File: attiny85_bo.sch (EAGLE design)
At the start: 11 parts, among them IC1 ATTiny85, J1 AVR_SPI_PRG_6NS, Y1 16MHz

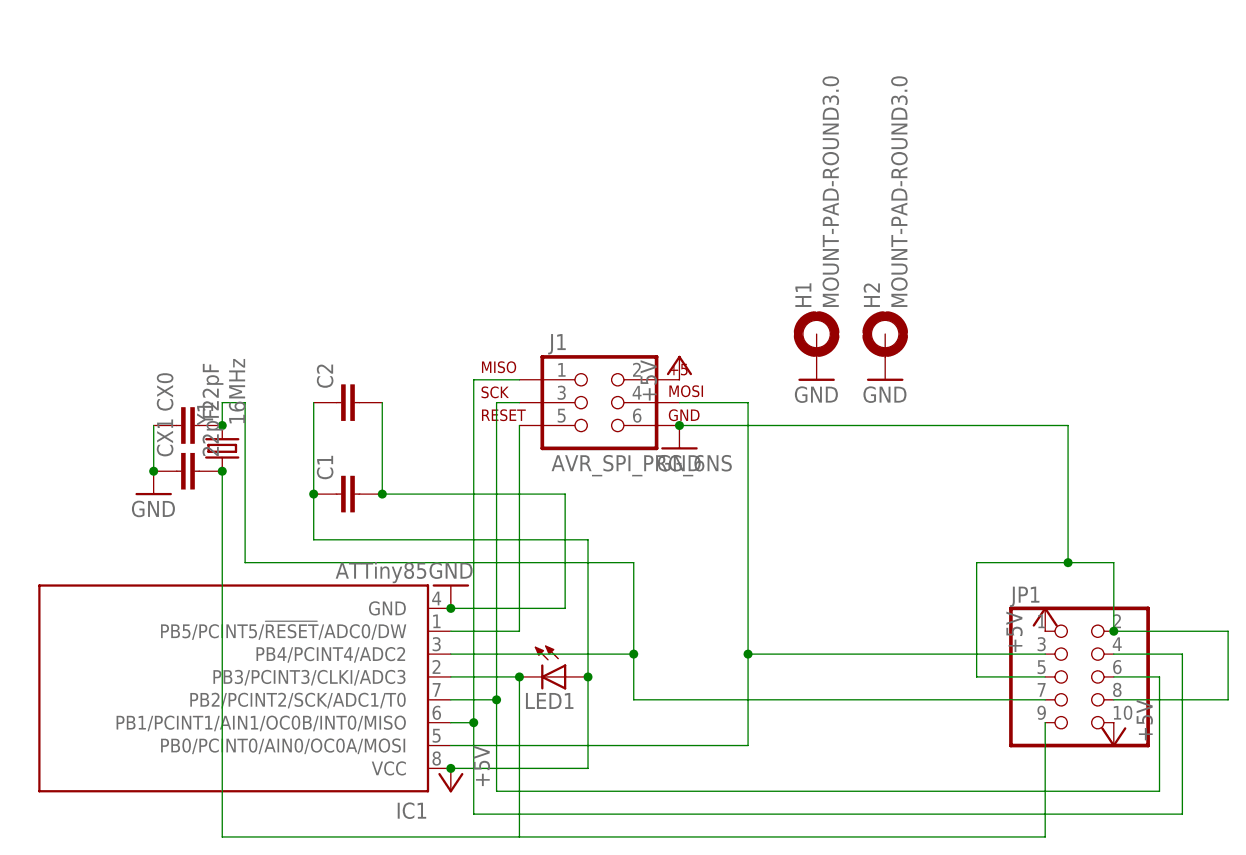
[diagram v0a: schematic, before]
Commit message: remaking the attiny85 baord so it is more easily connected to stripboard via 90deg pin header
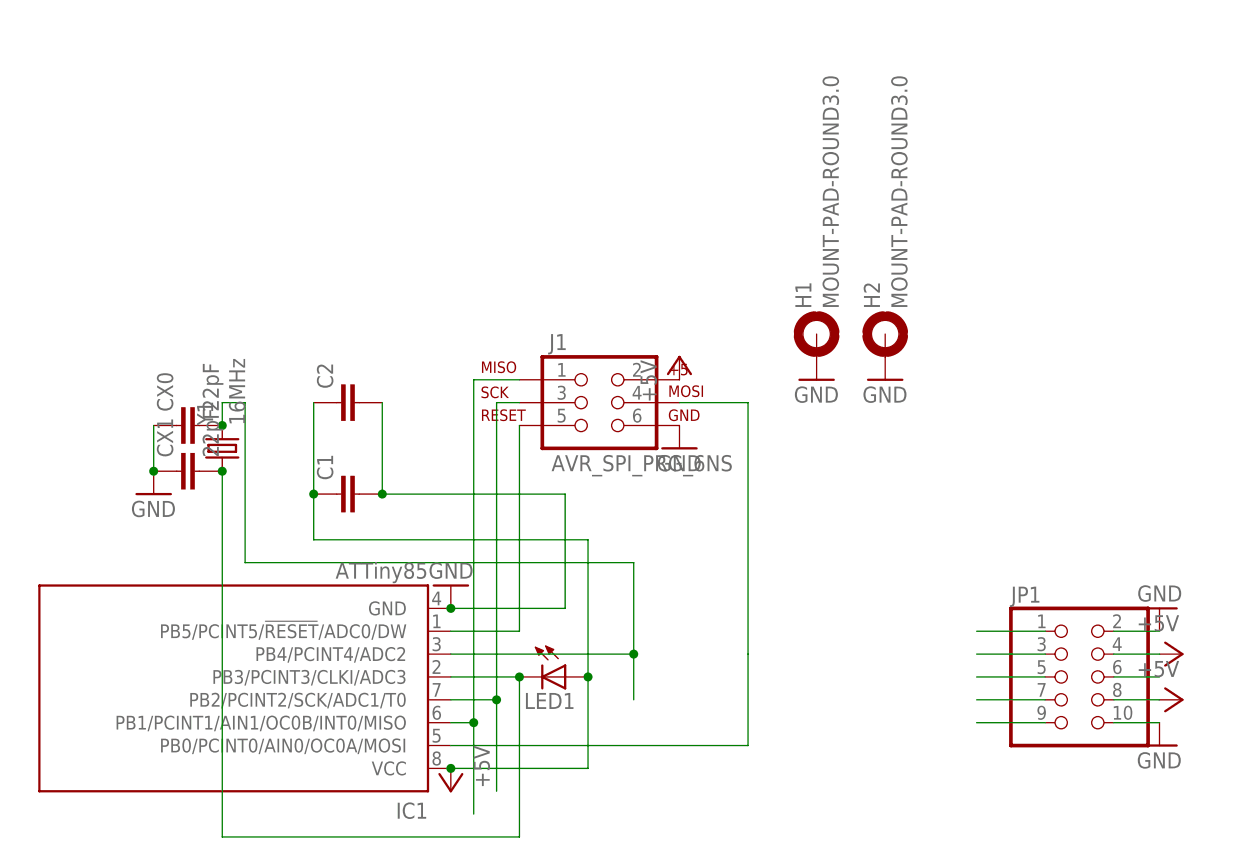
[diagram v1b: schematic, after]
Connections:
- net +5V: now also JP1.4, JP1.8; no longer JP1.1, JP1.10
- net GND: now also JP1.10; no longer JP1.5, JP1.8
- net PB0: now also JP1.1; no longer JP1.3
- net PB1: now also JP1.3; no longer JP1.4
- net PB2: now also JP1.5; no longer JP1.6
- net PB3: now also JP1.7; no longer JP1.9
- net PB4: now also JP1.9; no longer JP1.7
- net PB5: now also JP1.6
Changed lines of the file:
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@@
 <?xml version="1.0" encoding="utf-8"?>
 <!DOCTYPE eagle SYSTEM "eagle.dtd">
-<eagle version="6.2">
+<eagle version="6.4">
 <drawing>
 <settings>
@@
 <part name="GND1" library="supply1" deviceset="GND" device=""/>
 <part name="GND2" library="supply1" deviceset="GND" device=""/>
-<part name="P+1" library="supply1" deviceset="+5V" device=""/>
-<part name="P+2" library="supply1" deviceset="+5V" device=""/>
 <part name="CX0" library="rcl" deviceset="C-EU" device="C0603" value="22pF"/>
 <part name="CX1" library="rcl" deviceset="C-EU" device="C0603" value="22pF"/>
 <part name="GND4" library="supply1" deviceset="GND" device=""/>
 <part name="Y1" library="SparkFun-FreqCtrl" deviceset="CRYSTAL" device="5X3" value="16MHz"/>
+<part name="GND6" library="supply1" deviceset="GND" device=""/>
+<part name="GND7" library="supply1" deviceset="GND" device=""/>
+<part name="P+1" library="supply1" deviceset="+5V" device=""/>
+<part name="P+2" library="supply1" deviceset="+5V" device=""/>
 </parts>
 <sheets>
@@
 <instance part="GND1" gate="1" x="99.06" y="109.22"/>
 <instance part="GND2" gate="1" x="91.44" y="109.22"/>
-<instance part="P+1" gate="1" x="116.84" y="83.82"/>
-<instance part="P+2" gate="1" x="124.46" y="68.58" rot="R180"/>
 <instance part="CX0" gate="G$1" x="20.32" y="104.14" rot="R90"/>
 <instance part="CX1" gate="G$1" x="20.32" y="99.06" rot="R90"/>
 <instance part="GND4" gate="1" x="17.78" y="96.52"/>
 <instance part="Y1" gate="G$1" x="25.4" y="101.6" rot="R90"/>
+<instance part="GND6" gate="1" x="129.54" y="68.58"/>
+<instance part="GND7" gate="1" x="129.54" y="83.82" rot="R180"/>
+<instance part="P+1" gate="1" x="132.08" y="78.74" rot="R270"/>
+<instance part="P+2" gate="1" x="132.08" y="73.66" rot="R270"/>
 </instances>
 <busses>
@@
 <wire x1="58.42" y1="109.22" x2="53.34" y2="109.22" width="0.1524" layer="91"/>
 <wire x1="53.34" y1="109.22" x2="53.34" y2="71.12" width="0.1524" layer="91"/>
-<pinref part="JP1" gate="A" pin="4"/>
-<wire x1="124.46" y1="78.74" x2="132.08" y2="78.74" width="0.1524" layer="91"/>
-<wire x1="132.08" y1="78.74" x2="132.08" y2="60.96" width="0.1524" layer="91"/>
-<wire x1="132.08" y1="60.96" x2="53.34" y2="60.96" width="0.1524" layer="91"/>
 <wire x1="53.34" y1="60.96" x2="53.34" y2="71.12" width="0.1524" layer="91"/>
 <junction x="53.34" y="71.12"/>
+</segment>
+<segment>
+<pinref part="JP1" gate="A" pin="3"/>
+<wire x1="116.84" y1="78.74" x2="109.22" y2="78.74" width="0.1524" layer="91"/>
 </segment>
 </net>
@@
 <pinref part="J1" gate="G$1" pin="6"/>
 <pinref part="GND5" gate="1" pin="GND"/>
-<wire x1="76.2" y1="104.14" x2="119.38" y2="104.14" width="0.1524" layer="91"/>
-<wire x1="119.38" y1="104.14" x2="119.38" y2="88.9" width="0.1524" layer="91"/>
-<pinref part="JP1" gate="A" pin="2"/>
-<wire x1="124.46" y1="81.28" x2="124.46" y2="88.9" width="0.1524" layer="91"/>
-<wire x1="124.46" y1="88.9" x2="119.38" y2="88.9" width="0.1524" layer="91"/>
-<wire x1="119.38" y1="88.9" x2="109.22" y2="88.9" width="0.1524" layer="91"/>
-<wire x1="109.22" y1="88.9" x2="109.22" y2="76.2" width="0.1524" layer="91"/>
-<pinref part="JP1" gate="A" pin="5"/>
-<wire x1="109.22" y1="76.2" x2="116.84" y2="76.2" width="0.1524" layer="91"/>
-<wire x1="124.46" y1="81.28" x2="137.16" y2="81.28" width="0.1524" layer="91"/>
-<wire x1="137.16" y1="81.28" x2="137.16" y2="73.66" width="0.1524" layer="91"/>
-<pinref part="JP1" gate="A" pin="8"/>
-<wire x1="137.16" y1="73.66" x2="124.46" y2="73.66" width="0.1524" layer="91"/>
-<junction x="119.38" y="88.9"/>
-<junction x="76.2" y="104.14"/>
-<junction x="124.46" y="81.28"/>
 </segment>
 <segment>
@@
 <wire x1="17.78" y1="104.14" x2="17.78" y2="99.06" width="0.1524" layer="91"/>
 <junction x="17.78" y="99.06"/>
+</segment>
+<segment>
+<pinref part="JP1" gate="A" pin="10"/>
+<wire x1="124.46" y1="71.12" x2="129.54" y2="71.12" width="0.1524" layer="91"/>
+<pinref part="GND6" gate="1" pin="GND"/>
+</segment>
+<segment>
+<pinref part="JP1" gate="A" pin="2"/>
+<wire x1="124.46" y1="81.28" x2="129.54" y2="81.28" width="0.1524" layer="91"/>
+<pinref part="GND7" gate="1" pin="GND"/>
 </segment>
 </net>
@@
 </segment>
 <segment>
-<pinref part="JP1" gate="A" pin="1"/>
+<pinref part="JP1" gate="A" pin="4"/>
+<wire x1="124.46" y1="78.74" x2="129.54" y2="78.74" width="0.1524" layer="91"/>
 <pinref part="P+1" gate="1" pin="+5V"/>
 </segment>
 <segment>
-<pinref part="JP1" gate="A" pin="10"/>
+<pinref part="JP1" gate="A" pin="8"/>
+<wire x1="124.46" y1="73.66" x2="129.54" y2="73.66" width="0.1524" layer="91"/>
 <pinref part="P+2" gate="1" pin="+5V"/>
 </segment>
@@
 <wire x1="83.82" y1="78.74" x2="83.82" y2="106.68" width="0.1524" layer="91"/>
 <wire x1="83.82" y1="106.68" x2="76.2" y2="106.68" width="0.1524" layer="91"/>
-<pinref part="JP1" gate="A" pin="3"/>
-<wire x1="116.84" y1="78.74" x2="83.82" y2="78.74" width="0.1524" layer="91"/>
-<junction x="83.82" y="78.74"/>
+</segment>
+<segment>
+<pinref part="JP1" gate="A" pin="1"/>
+<wire x1="116.84" y1="81.28" x2="109.22" y2="81.28" width="0.1524" layer="91"/>
 </segment>
 </net>
@@
 <wire x1="50.8" y1="81.28" x2="58.42" y2="81.28" width="0.1524" layer="91"/>
 <wire x1="58.42" y1="81.28" x2="58.42" y2="104.14" width="0.1524" layer="91"/>
+</segment>
+<segment>
+<pinref part="JP1" gate="A" pin="6"/>
+<wire x1="124.46" y1="76.2" x2="129.54" y2="76.2" width="0.1524" layer="91"/>
 </segment>
 </net>
@@
 <pinref part="J1" gate="G$1" pin="3"/>
 <wire x1="55.88" y1="106.68" x2="58.42" y2="106.68" width="0.1524" layer="91"/>
-<pinref part="JP1" gate="A" pin="6"/>
-<wire x1="124.46" y1="76.2" x2="129.54" y2="76.2" width="0.1524" layer="91"/>
-<wire x1="129.54" y1="76.2" x2="129.54" y2="63.5" width="0.1524" layer="91"/>
-<wire x1="129.54" y1="63.5" x2="55.88" y2="63.5" width="0.1524" layer="91"/>
 <wire x1="55.88" y1="63.5" x2="55.88" y2="73.66" width="0.1524" layer="91"/>
 <junction x="55.88" y="73.66"/>
+</segment>
+<segment>
+<pinref part="JP1" gate="A" pin="5"/>
+<wire x1="116.84" y1="76.2" x2="109.22" y2="76.2" width="0.1524" layer="91"/>
 </segment>
 </net>
@@
 <wire x1="58.42" y1="76.2" x2="50.8" y2="76.2" width="0.1524" layer="91"/>
 <wire x1="58.42" y1="76.2" x2="58.42" y2="58.42" width="0.1524" layer="91"/>
-<pinref part="JP1" gate="A" pin="9"/>
-<wire x1="58.42" y1="58.42" x2="116.84" y2="58.42" width="0.1524" layer="91"/>
-<wire x1="116.84" y1="58.42" x2="116.84" y2="71.12" width="0.1524" layer="91"/>
 <junction x="58.42" y="76.2"/>
 <pinref part="CX1" gate="G$1" pin="2"/>
@@
 <junction x="25.4" y="99.06"/>
 </segment>
+<segment>
+<pinref part="JP1" gate="A" pin="7"/>
+<wire x1="116.84" y1="73.66" x2="109.22" y2="73.66" width="0.1524" layer="91"/>
+</segment>
 </net>
 <net name="PB4" class="0">
@@
 <wire x1="50.8" y1="78.74" x2="71.12" y2="78.74" width="0.1524" layer="91"/>
 <wire x1="71.12" y1="78.74" x2="71.12" y2="73.66" width="0.1524" layer="91"/>
-<pinref part="JP1" gate="A" pin="7"/>
-<wire x1="71.12" y1="73.66" x2="116.84" y2="73.66" width="0.1524" layer="91"/>
 <wire x1="71.12" y1="78.74" x2="71.12" y2="88.9" width="0.1524" layer="91"/>
 <wire x1="71.12" y1="88.9" x2="27.94" y2="88.9" width="0.1524" layer="91"/>
@@
 <junction x="25.4" y="104.14"/>
 </segment>
-</net>
+<segment>
+<pinref part="JP1" gate="A" pin="9"/>
+<wire x1="116.84" y1="71.12" x2="109.22" y2="71.12" width="0.1524" layer="91"/>
+</segment>
+</net>
